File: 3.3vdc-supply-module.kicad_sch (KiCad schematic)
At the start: 0 parts

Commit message: Place Holder:
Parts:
- added F?: Fuse, symbol Device:Fuse
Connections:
- new net 3.3VDC_FUSED_SUPPLY: F?.2
- new net 3.3VDC_SUPPLY: F?.1
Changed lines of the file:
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@@
     (company "eatmellc")
   )
+  (global_label "3.3VDC_SUPPLY" (shape input) (at 78.74 64.77 180) (fields_autoplaced)
+    (effects (font (size 1.27 1.27)) (justify right))
+    (property "Intersheet References" "${INTERSHEET_REFS}" (id 0) (at 61.5102 64.6906 0)
+      (effects (font (size 1.27 1.27)) (justify right))
+    )
+  )
+  (global_label "3.3VDC_FUSED_SUPPLY" (shape input) (at 86.36 64.77 0) (fields_autoplaced)
+    (effects (font (size 1.27 1.27)) (justify left))
+    (property "Intersheet References" "${INTERSHEET_REFS}" (id 0) (at 110.605 64.6906 0)
+      (effects (font (size 1.27 1.27)) (justify left))
+    )
+  )
+  (symbol (lib_id "Device:Fuse") (at 82.55 64.77 90) (unit 1)
+    (in_bom yes) (on_board yes) (fields_autoplaced)
+    (property "Reference" "F?" (id 0) (at 82.55 58.42 90))
+    (property "Value" "Fuse" (id 1) (at 82.55 60.96 90))
+    (property "Footprint" "" (id 2) (at 82.55 66.548 90)
+      (effects (font (size 1.27 1.27)) hide)
+    )
+    (property "Datasheet" "~" (id 3) (at 82.55 64.77 0)
+      (effects (font (size 1.27 1.27)) hide)
+    )
+    (pin "1")
+    (pin "2")
+  )
 )

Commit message: Draft 5VDC Supply Schematic
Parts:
- gave numbers to parts that had none: 1
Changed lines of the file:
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@@
   (symbol (lib_id "Device:Fuse") (at 82.55 64.77 90) (unit 1)
     (in_bom yes) (on_board yes) (fields_autoplaced)
-    (property "Reference" "F?" (id 0) (at 82.55 58.42 90))
+    (property "Reference" "F5" (id 0) (at 82.55 58.42 90))
     (property "Value" "Fuse" (id 1) (at 82.55 60.96 90))
     (property "Footprint" "" (id 2) (at 82.55 66.548 90)

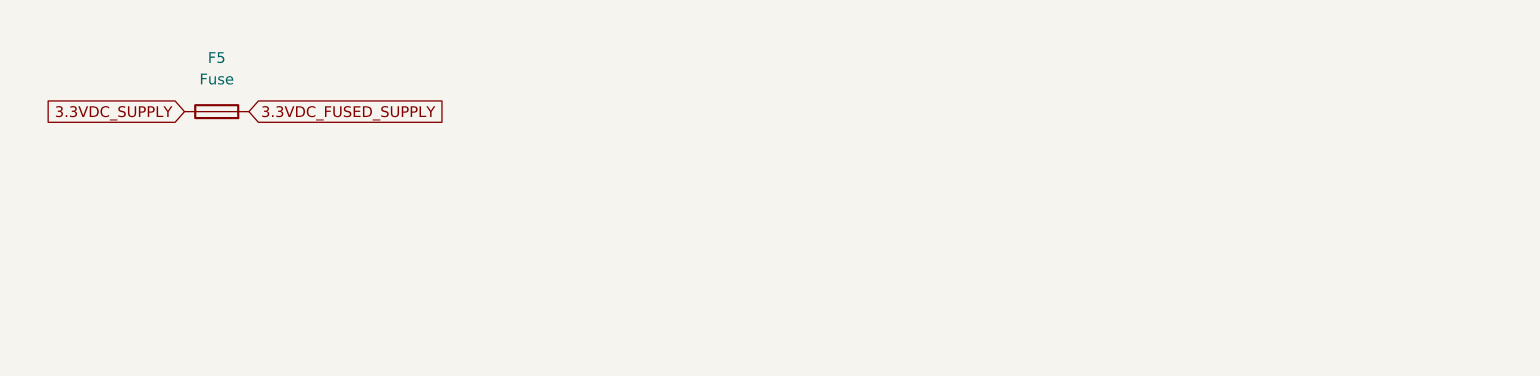
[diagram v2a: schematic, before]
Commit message: Save more changes
Started Fan Control
Created VDC Meter Template
Fleshed out 12, 5, 5-usb, and 3.3 modules
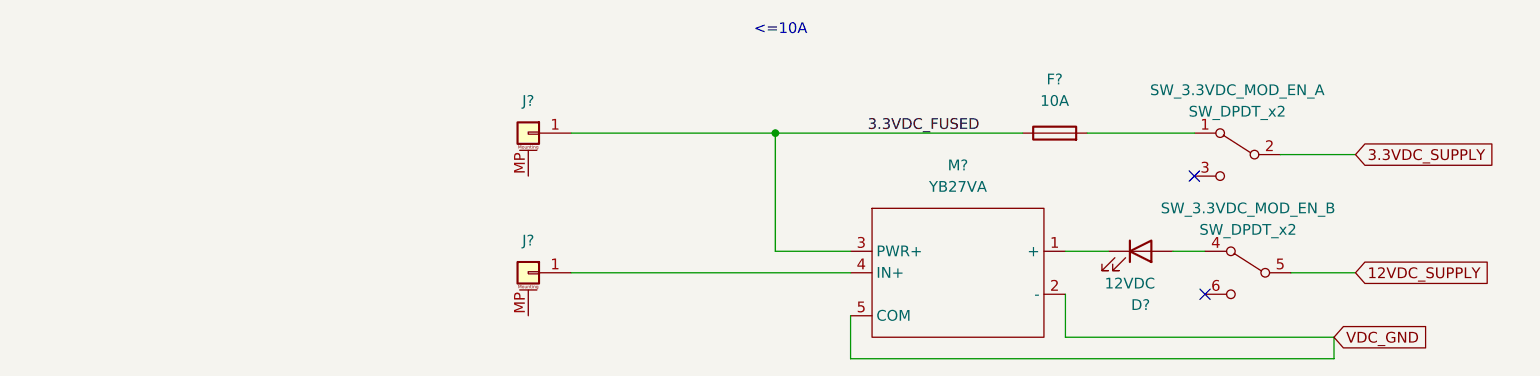
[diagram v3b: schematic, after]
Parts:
- removed F5: Fuse, symbol Device:Fuse
- added D?: 12VDC, symbol Device:LED
- added F?: 10A, symbol Device:Fuse
- added J? (x2): Conn_01x01_MountingPin, symbol Connector_Generic_MountingPin:Conn_01x01_MountingPin
- added M?: YB27VA, symbol bvm-library:5_Pin_Meter_With_Ext_Shunt
- added SW_3.3VDC_MOD_EN_: SW_DPDT_x2, symbol Switch:SW_DPDT_x2
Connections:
- net 3.3VDC_SUPPLY: now also SW_3.3VDC_MOD_EN_.2 (B)
- new net: D?.1 (K), M?.1 (+)
- new net: J?.1 (Pin_1), M?.4 (IN+)
- new net: D?.2 (A), SW_3.3VDC_MOD_EN_.4 (A)
- new net: F?.2, SW_3.3VDC_MOD_EN_.1 (A)
- new net 12VDC_SUPPLY: SW_3.3VDC_MOD_EN_.5 (B)
- new net 3.3VDC_FUSED: F?.1, J?.1 (Pin_1), M?.3 (PWR+)
- new net VDC_GND: M?.2 (-), M?.5 (COM)
- no-connect marks 0 -> 2
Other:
- note added: "<=10A"

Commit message: Bunch more changes
Blah blah
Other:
- title: (none) -> Mr. Powers
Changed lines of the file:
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@@
   (paper "A4")
   (title_block
+    (title "Mr. Powers")
     (date "2022-05-20")
     (rev "0.0.0-draft")

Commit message: Minor change across the board
I need better notes.
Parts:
- added D?: LED, symbol Device:LED
- added F?: 10A, symbol Device:Fuse
- added M?: YB27VA, symbol bvm-library:5_Pin_Meter_With_Ext_Shunt
- added SW_3.3VDC_USB_MOD_EN?: SW_SPST_LED_3pin, symbol bvm-library:SW_SPST_LED_3pin
- gave numbers to parts that had none: 5
- renumbered SW_3.3VDC_MOD_EN_ to SW_3.3VDC_MOD_EN_1
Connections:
- net 12VDC_SUPPLY: now also M?.1 (+)
- net 3.3VDC_SUPPLY: now also SW_3.3VDC_USB_MOD_EN?.2
- net VDC_GND: now also D?.1 (K), M?.2 (-), M?.5 (COM), SW_3.3VDC_USB_MOD_EN?.3 (A)
- new net: F?.2, SW_3.3VDC_USB_MOD_EN?.1
- new net 3.3VDC_USB_FUSED: D?.2 (A), F?.1, M?.3 (PWR+)
- new net GND: M?.4 (IN+)
- no-connect marks 2 -> 3
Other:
- note added: "[3.3VDC USB MODULE ACTIVE]"
